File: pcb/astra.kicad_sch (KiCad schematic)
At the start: 0 parts

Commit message: add subsheets
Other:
- added sheet Camera (camera.kicad_sch)
- added sheet MCU (mcu.kicad_sch)
- added sheet Motor Controller (motor-controller.kicad_sch)
- added sheet Motor Controller1 (motor-controller.kicad_sch)
- added sheet Motor Controller2 (motor-controller.kicad_sch)
- added sheet Motor Controller3 (motor-controller.kicad_sch)

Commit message: [journal] add 6/10 schematic entry
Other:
- removed sheet Motor Controller1
- removed sheet Motor Controller2
- removed sheet Motor Controller3
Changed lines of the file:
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@@
-	)
-	(sheet
-		(at 119.38 17.78)
-		(size 25.4 15.24)
-		(exclude_from_sim no)
-		(in_bom yes)
-		(on_board yes)
-		(dnp no)
-		(fields_autoplaced yes)
-		(stroke
-			(width 0.1524)
-			(type solid)
-		)
-		(fill
-			(color 0 0 0 0.0000)
-		)
-		(property "Sheetname" "Motor Controller2"
-			(at 119.38 17.0684 0)
-			(effects
-				(font
-					(size 1.27 1.27)
-				)
-				(justify left bottom)
-			)
-		)
-		(property "Sheetfile" "motor-controller.kicad_sch"
-			(at 119.38 33.6046 0)
-			(effects
-				(font
-					(size 1.27 1.27)
-				)
-				(justify left top)
-			)
-		)
-		(instances
-			(project "astra"
-				(path "/c0be3de2-9de4-4447-aa6f-537ea5f31aac"
-					(page "5")
-				)
-			)
-		)
 	)
 	(sheet
@@
 	)
 	(sheet
-		(at 83.82 17.78)
-		(size 25.4 15.24)
-		(exclude_from_sim no)
-		(in_bom yes)
-		(on_board yes)
-		(dnp no)
-		(fields_autoplaced yes)
-		(stroke
-			(width 0.1524)
-			(type solid)
-		)
-		(fill
-			(color 0 0 0 0.0000)
-		)
-		(property "Sheetname" "Motor Controller1"
-			(at 83.82 17.0684 0)
-			(effects
-				(font
-					(size 1.27 1.27)
-				)
-				(justify left bottom)
-			)
-		)
-		(property "Sheetfile" "motor-controller.kicad_sch"
-			(at 83.82 33.6046 0)
-			(effects
-				(font
-					(size 1.27 1.27)
-				)
-				(justify left top)
-			)
-		)
-		(instances
-			(project "astra"
-				(path "/c0be3de2-9de4-4447-aa6f-537ea5f31aac"
-					(page "4")
-				)
-			)
-		)
-	)
-	(sheet
 		(at 50.8 17.78)
 		(size 25.4 15.24)
@@
 				)
 			)
-		)
-	)
-	(sheet
-		(at 154.94 17.78)
-		(size 25.4 15.24)
-		(exclude_from_sim no)
-		(in_bom yes)
-		(on_board yes)
-		(dnp no)
-		(fields_autoplaced yes)
-		(stroke
-			(width 0.1524)
-			(type solid)
-		)
-		(fill
-			(color 0 0 0 0.0000)
-		)
-		(property "Sheetname" "Motor Controller3"
-			(at 154.94 17.0684 0)
-			(effects
-				(font
-					(size 1.27 1.27)
-				)
-				(justify left bottom)
-			)
-		)
-		(property "Sheetfile" "motor-controller.kicad_sch"
-			(at 154.94 33.6046 0)
-			(effects
-				(font
-					(size 1.27 1.27)
-				)
-				(justify left top)
-			)
-		)
-		(instances
-			(project "astra"
-				(path "/c0be3de2-9de4-4447-aa6f-537ea5f31aac"
-					(page "6")
-				)
-			)

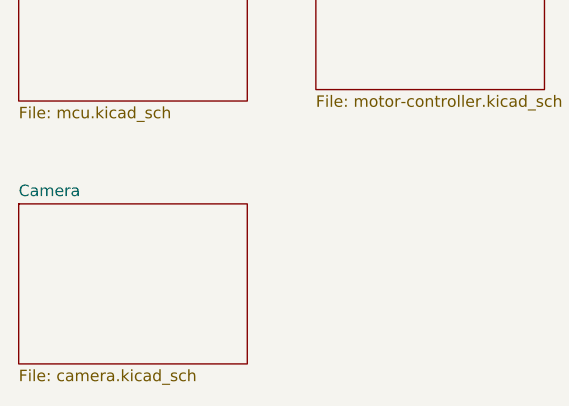
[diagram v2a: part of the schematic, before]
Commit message: [pcb] start transceiver implementation
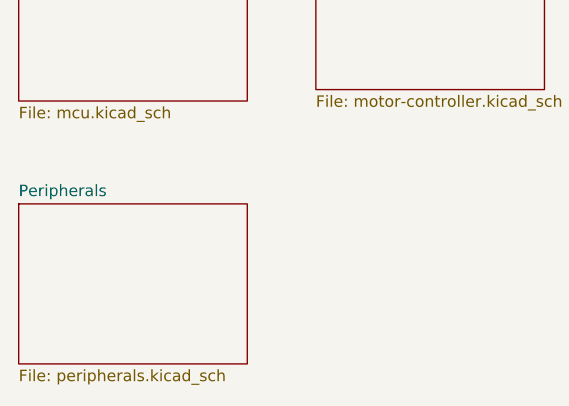
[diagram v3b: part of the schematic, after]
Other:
- removed sheet Camera
- added sheet Peripherals (peripherals.kicad_sch)
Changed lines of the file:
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@@
 			(color 0 0 0 0.0000)
 		)
-		(property "Sheetname" "Camera"
+		(property "Sheetname" "Peripherals"
 			(at 17.78 45.0084 0)
 			(effects
@@
 			)
 		)
-		(property "Sheetfile" "camera.kicad_sch"
+		(property "Sheetfile" "peripherals.kicad_sch"
 			(at 17.78 64.0846 0)
 			(effects
@@
 			(project "astra"
 				(path "/c0be3de2-9de4-4447-aa6f-537ea5f31aac"
-					(page "7")
+					(page "4")
 				)
 			)
